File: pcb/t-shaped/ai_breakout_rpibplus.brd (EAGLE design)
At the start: 58.4 x 64.8 mm, 5 parts, among them J1 1X20, J2 1X20NOFIRST, J3 2X20-RPI-BRK

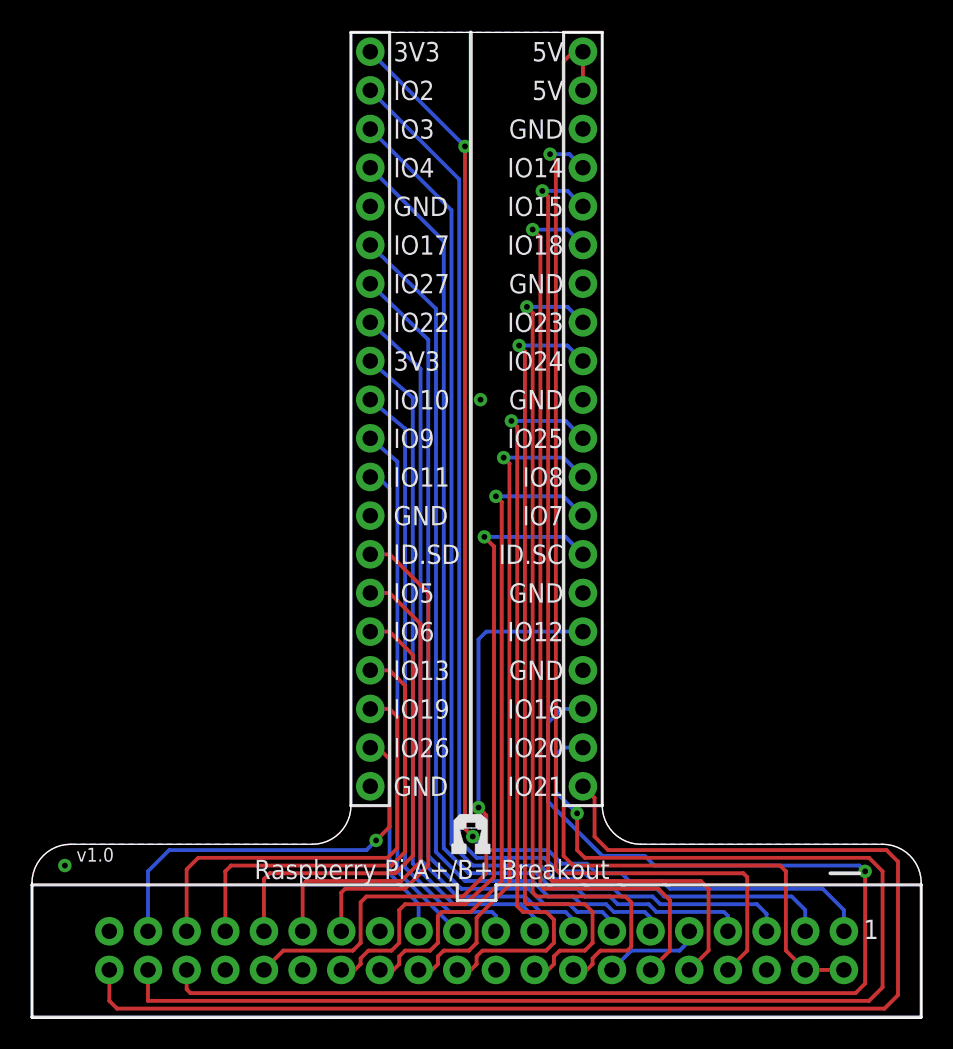
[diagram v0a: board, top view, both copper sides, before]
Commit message: Updating T-Shaped.  Added a few labels to R-Shaped
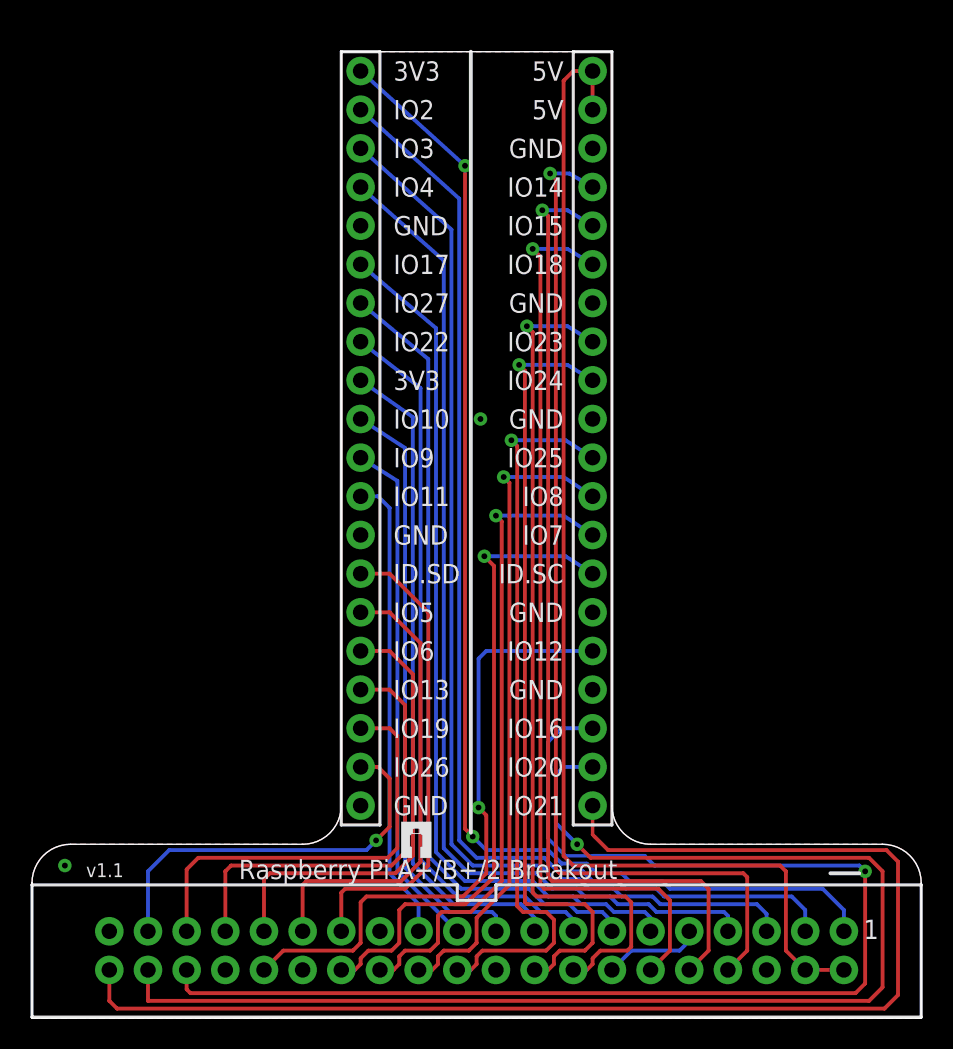
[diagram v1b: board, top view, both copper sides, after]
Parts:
- moved U$2 3.44 mm to (33.5, 10.5)
- moved U$1 3.31 mm to (24.3, 10.5)
- moved J1 1.42 mm to (21.6, 38.1)
- moved J2 1.42 mm to (36.8, 38.1)
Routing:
- net N$46: track 87.4 -> 85.9 mm
- net N$45: track 87.7 -> 86.9 mm
- net N$21: track 82.1 -> 81.3 mm
- net N$22: track 77.7 -> 76.9 mm
- net N$23: track 72.9 -> 72.1 mm
- net N$24: track 68.2 -> 67.4 mm
- net N$26: track 58.5 -> 57.7 mm
- net N$20: track 53.7 -> 52.9 mm
- net N$19: track 49.2 -> 48.4 mm
- net N$44: track 84.2 -> 84.9 mm
- net N$38: track 43.5 -> 42.7 mm
- net N$39: track 43.4 -> 42.7 mm
- net N$37: track 48.9 -> 48.1 mm
- net N$40: track 43.6 -> 42.8 mm
- net N$18: track 44.7 -> 43.9 mm
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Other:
- board size 58.4 x 64.8 mm -> 58.4 x 63.5 mm
- board text added: "Raspberry Pi A+/B+/2 Breakout"
- board text added: "https://acrobotic.com"
- board text added: "v1.1"
- board text removed: "Raspberry Pi A+/B+ Breakout"
- board text removed: "v1.0"
